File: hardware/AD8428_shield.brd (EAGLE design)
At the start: 17.4 x 10.2 mm, 3 parts, among them U1 AD8428ARZ

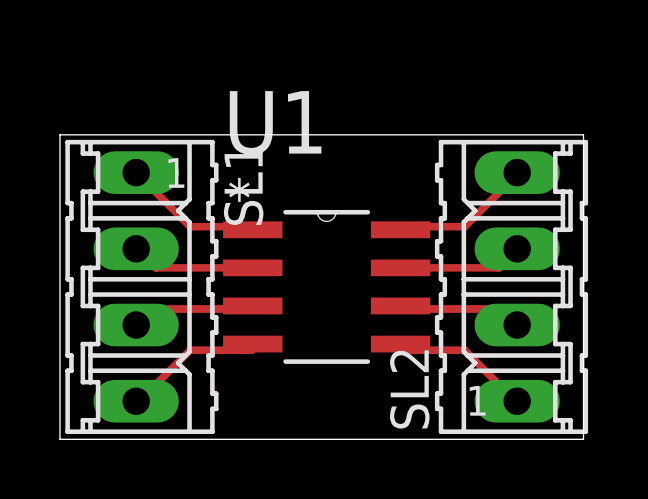
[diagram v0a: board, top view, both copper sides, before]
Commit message: updated AD8428 shield
- added text to board
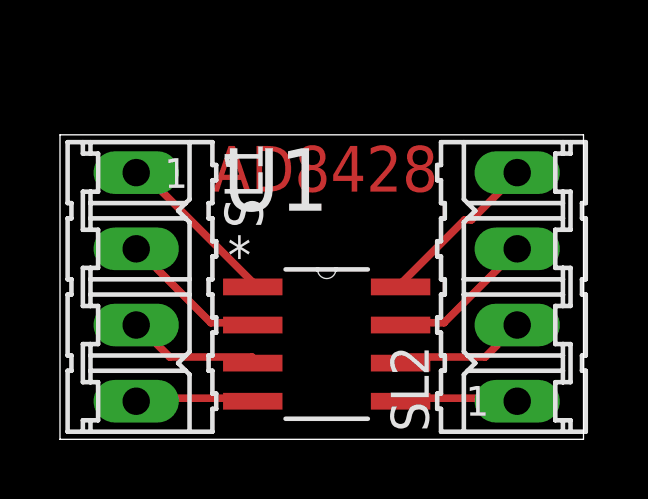
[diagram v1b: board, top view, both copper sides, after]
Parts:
- moved U1 1.91 mm to (8.89, 3.17)
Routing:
- net N$1: track 4.71 -> 5.56 mm
- net N$8: track 4.70 -> 5.53 mm
- net N$2: track 4.14 -> 4.95 mm
- net N$7: track 4.16 -> 4.95 mm
- net N$4: track 4.75 -> 3.99 mm
- net N$5: track 4.72 -> 3.97 mm
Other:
- board text added: "AD8428"
